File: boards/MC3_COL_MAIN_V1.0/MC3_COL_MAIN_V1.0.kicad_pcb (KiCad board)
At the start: 4 copper layers, 66 x 66 mm, 0 parts

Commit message: PCB: 101 footprints imported from the schematic via Konnect update_pcb_from_schematic (IPC), saved from KiCad; not yet placed
Co-Authored-By: Claude Fable 5 <noreply@anthropic.com>
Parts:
- added C1: 10uF, MC3_COL_MAIN:C_0805_2012Metric, F.Cu at (6.70, 25.0)
- added C10: 100nF, MC3_COL_MAIN:C_0402_1005Metric, F.Cu at (5.91, 154.6)
- added C11: 1uF, MC3_COL_MAIN:C_0402_1005Metric, F.Cu at (5.91, 160.6)
- added C12: 33pF, MC3_COL_MAIN:C_0402_1005Metric, F.Cu at (5.91, 166.6)
- added C13: 100nF, MC3_COL_MAIN:C_0402_1005Metric, F.Cu at (5.91, 172.6)
- added C14: 4.7uF, MC3_COL_MAIN:C_0603_1608Metric, F.Cu at (6.48, 178.9)
- added C15: 100nF, MC3_COL_MAIN:C_0402_1005Metric, F.Cu at (5.91, 185.1)
- added C16: 4.7uF, MC3_COL_MAIN:C_0805_2012Metric, F.Cu at (6.70, 191.6)
- added C17: 4.7uF, MC3_COL_MAIN:C_0603_1608Metric, F.Cu at (6.48, 350.0)
- added C18: 1uF, MC3_COL_MAIN:C_0603_1608Metric, F.Cu at (6.48, 434.1)
- added C19: 100nF, MC3_COL_MAIN:C_0402_1005Metric, F.Cu at (5.91, 440.3)
- added C2: 22uF 10V Ta, MC3_COL_MAIN:CP_EIA-3216-18_Kemet-A, F.Cu at (7.31, 32.0)
- added C20: 1uF, MC3_COL_MAIN:C_0603_1608Metric, F.Cu at (6.48, 483.7)
- added C21: 100nF, MC3_COL_MAIN:C_0402_1005Metric, F.Cu at (5.91, 489.9)
- added C22: 1uF, MC3_COL_MAIN:C_0603_1608Metric, F.Cu at (6.48, 533.3)
- added C23: 100nF, MC3_COL_MAIN:C_0402_1005Metric, F.Cu at (5.91, 539.6)
- added C24: 1uF, MC3_COL_MAIN:C_0603_1608Metric, F.Cu at (6.48, 582.9)
- added C25: 100nF, MC3_COL_MAIN:C_0402_1005Metric, F.Cu at (5.91, 589.2)
- added C26: 1uF, MC3_COL_MAIN:C_0603_1608Metric, F.Cu at (6.48, 632.6)
- added C27: 100nF, MC3_COL_MAIN:C_0402_1005Metric, F.Cu at (5.91, 638.8)
- added C28: 100nF, MC3_COL_MAIN:C_0402_1005Metric, F.Cu at (5.91, 682.0)
- added C29: 4.7uF, MC3_COL_MAIN:C_0603_1608Metric, F.Cu at (6.48, 688.2)
- added C3: 22uF 25V, MC3_COL_MAIN:C_0805_2012Metric, F.Cu at (6.70, 39.0)
- added C30: 4.7nF, MC3_COL_MAIN:C_0402_1005Metric, F.Cu at (5.91, 694.4)
- added C4: 22uF 25V, MC3_COL_MAIN:C_0805_2012Metric, F.Cu at (6.70, 46.0)
- added C5: 100nF, MC3_COL_MAIN:C_0402_1005Metric, F.Cu at (5.91, 124.6)
- added C6: 100nF, MC3_COL_MAIN:C_0402_1005Metric, F.Cu at (5.91, 130.6)
- added C7: 100nF, MC3_COL_MAIN:C_0402_1005Metric, F.Cu at (5.91, 136.6)
- added C8: 33pF, MC3_COL_MAIN:C_0402_1005Metric, F.Cu at (5.91, 142.6)
- added C9: 100nF, MC3_COL_MAIN:C_0402_1005Metric, F.Cu at (5.91, 148.6)
- added D1: SMAJ5.0A, MC3_COL_MAIN:D_SMA, F.Cu at (8.50, 54.4)
- added D2: LED_GREEN, MC3_COL_MAIN:LED_0603_1608Metric, F.Cu at (6.48, 198.3)
- added D3: LED_RED, MC3_COL_MAIN:LED_0603_1608Metric, F.Cu at (6.48, 204.8)
- added D4: PESD1CAN, MC3_COL_MAIN:SOT-23, F.Cu at (6.93, 701.6)
- added F1: 2A hold/3.5A trip, MC3_COL_MAIN:Fuse_1206_3216Metric, F.Cu at (7.28, 62.9)
- added FB1: 600R@100MHz, MC3_COL_MAIN:L_0603_1608Metric, F.Cu at (6.48, 211.2)
- added FB2: 600R@100MHz, MC3_COL_MAIN:L_0603_1608Metric, F.Cu at (6.48, 356.4)
- added FB3: 600R@100MHz, MC3_COL_MAIN:L_0603_1608Metric, F.Cu at (6.48, 709.0)
- added J1: SUPPLY_IN, MC3_COL_MAIN:SolderPads_2x_3.5x2.0mm_P4.2mm, F.Cu at (9.32, 71.7)
- added J10: MOTOR, MC3_COL_MAIN:SolderPads_2x_2.2x1.4mm_P2.6mm, F.Cu at (7.88, 597.1)
- added J11: MOTOR, MC3_COL_MAIN:SolderPads_2x_2.2x1.4mm_P2.6mm, F.Cu at (7.88, 646.8)
- added J12: CAN, MC3_COL_MAIN:SolderPads_3x_2.2x1.4mm_P2.6mm, F.Cu at (9.18, 717.2)
- added J2: SWD, MC3_COL_MAIN:PinHeader_1x06_P2.54mm_Vertical, F.Cu at (6.77, 225.1)
- added J3: ENC_leaf1, MC3_COL_MAIN:Panasonic_AYF530435_FFC-4P_P0.5mm, F.Cu at (7.20, 365.6)
- added J4: ENC_leaf2, MC3_COL_MAIN:Panasonic_AYF530435_FFC-4P_P0.5mm, F.Cu at (7.20, 377.4)
- added J5: ENC_leaf3, MC3_COL_MAIN:Panasonic_AYF530435_FFC-4P_P0.5mm, F.Cu at (7.20, 389.2)
- added J6: ENC_leaf4, MC3_COL_MAIN:Panasonic_AYF530435_FFC-4P_P0.5mm, F.Cu at (7.20, 401.0)
- added J7: MOTOR, MC3_COL_MAIN:SolderPads_2x_2.2x1.4mm_P2.6mm, F.Cu at (7.88, 448.3)
- added J8: MOTOR, MC3_COL_MAIN:SolderPads_2x_2.2x1.4mm_P2.6mm, F.Cu at (7.88, 497.9)
- added J9: MOTOR, MC3_COL_MAIN:SolderPads_2x_2.2x1.4mm_P2.6mm, F.Cu at (7.88, 547.5)
- added Q1: AO4407C, MC3_COL_MAIN:SOIC-8_3.9x4.9mm_P1.27mm, F.Cu at (8.70, 82.2)
- added R1: 2.2k, MC3_COL_MAIN:R_0402_1005Metric, F.Cu at (5.93, 0.50)
- added R10: 1k, MC3_COL_MAIN:R_0402_1005Metric, F.Cu at (5.93, 262.7)
- added R11: 1k, MC3_COL_MAIN:R_0402_1005Metric, F.Cu at (5.93, 268.7)
- added R12: 10k, MC3_COL_MAIN:R_0402_1005Metric, F.Cu at (5.93, 409.9)
- added R13: 10k, MC3_COL_MAIN:R_0402_1005Metric, F.Cu at (5.93, 415.9)
- added R14: 10k, MC3_COL_MAIN:R_0402_1005Metric, F.Cu at (5.93, 421.9)
- added R15: 10k, MC3_COL_MAIN:R_0402_1005Metric, F.Cu at (5.93, 427.9)
- added R16: 6.8k, MC3_COL_MAIN:R_0402_1005Metric, F.Cu at (5.93, 456.2)
- added R17: 10k, MC3_COL_MAIN:R_0402_1005Metric, F.Cu at (5.93, 462.2)
- added R18: 10k, MC3_COL_MAIN:R_0402_1005Metric, F.Cu at (5.93, 468.2)
- added R19: 6.8k, MC3_COL_MAIN:R_0402_1005Metric, F.Cu at (5.93, 505.8)
- added R2: 2.2k, MC3_COL_MAIN:R_0402_1005Metric, F.Cu at (5.93, 6.50)
- added R20: 10k, MC3_COL_MAIN:R_0402_1005Metric, F.Cu at (5.93, 511.8)
- added R21: 10k, MC3_COL_MAIN:R_0402_1005Metric, F.Cu at (5.93, 517.8)
- added R22: 6.8k, MC3_COL_MAIN:R_0402_1005Metric, F.Cu at (5.93, 555.5)
- added R23: 10k, MC3_COL_MAIN:R_0402_1005Metric, F.Cu at (5.93, 561.5)
- added R24: 10k, MC3_COL_MAIN:R_0402_1005Metric, F.Cu at (5.93, 567.5)
- added R25: 6.8k, MC3_COL_MAIN:R_0402_1005Metric, F.Cu at (5.93, 605.1)
- added R26: 10k, MC3_COL_MAIN:R_0402_1005Metric, F.Cu at (5.93, 611.1)
- added R27: 10k, MC3_COL_MAIN:R_0402_1005Metric, F.Cu at (5.93, 617.1)
- added R28: 6.8k, MC3_COL_MAIN:R_0402_1005Metric, F.Cu at (5.93, 654.7)
- added R29: 10k, MC3_COL_MAIN:R_0402_1005Metric, F.Cu at (5.93, 660.7)
- added R3: 2.2k, MC3_COL_MAIN:R_0402_1005Metric, F.Cu at (5.93, 12.5)
- added R30: 10k, MC3_COL_MAIN:R_0402_1005Metric, F.Cu at (5.93, 666.7)
- added R31: 62R, MC3_COL_MAIN:R_0402_1005Metric, F.Cu at (5.93, 725.2)
- added R32: 62R, MC3_COL_MAIN:R_0402_1005Metric, F.Cu at (5.93, 731.2)
- added R4: 2.2k, MC3_COL_MAIN:R_0402_1005Metric, F.Cu at (5.93, 18.5)
- added R5: 100k, MC3_COL_MAIN:R_0402_1005Metric, F.Cu at (5.93, 90.5)
- added R6: 4.7k, MC3_COL_MAIN:R_0402_1005Metric, F.Cu at (5.93, 238.7)
- added R7: 4.7k, MC3_COL_MAIN:R_0402_1005Metric, F.Cu at (5.93, 244.7)
- added R72: 0R, MC3_COL_MAIN:R_0402_1005Metric, F.Cu at (5.93, 737.2)
- added R8: 10k, MC3_COL_MAIN:R_0402_1005Metric, F.Cu at (5.93, 250.7)
- added R9: 10k, MC3_COL_MAIN:R_0402_1005Metric, F.Cu at (5.93, 256.7)
- added SW1: SKRKAEE020, MC3_COL_MAIN:SW_Push_SPST_NO_Alps_SKRK, F.Cu at (7.75, 275.9)
- added TP1: VM, MC3_COL_MAIN:TestPoint_Pad_1.0x1.0mm, F.Cu at (6.00, 97.5)
- added TP2: VIN_PROT, MC3_COL_MAIN:TestPoint_Pad_1.0x1.0mm, F.Cu at (6.00, 105.4)
- added TP3: +3V3, MC3_COL_MAIN:TestPoint_Pad_1.0x1.0mm, F.Cu at (6.00, 284.1)
- added TP4: SCL, MC3_COL_MAIN:TestPoint_Pad_1.0x1.0mm, F.Cu at (6.00, 292.0)
- added TP5: SDA, MC3_COL_MAIN:TestPoint_Pad_1.0x1.0mm, F.Cu at (6.00, 300.0)
- added TP6: IPROPI1, MC3_COL_MAIN:TestPoint_Pad_1.0x1.0mm, F.Cu at (6.00, 307.9)
- added TP7: GND, MC3_COL_MAIN:TestPoint_Pad_1.0x1.0mm, F.Cu at (6.00, 315.9)
- added U1: AMS1117-3.3, MC3_COL_MAIN:SOT-223-3_TabPin2, F.Cu at (9.40, 115.5)
- added U2: STM32F412RET6, MC3_COL_MAIN:LQFP-64_10x10mm_P0.5mm, F.Cu at (11.7, 329.0)
- added U3: DRV8214RTER, MC3_COL_MAIN:WQFN-16-1EP_3x3mm_P0.5mm_EP1.68x1.68mm_ThermalVias, F.Cu at (7.30, 475.8)
- added U4: DRV8214RTER, MC3_COL_MAIN:WQFN-16-1EP_3x3mm_P0.5mm_EP1.68x1.68mm_ThermalVias, F.Cu at (7.30, 525.5)
- added U5: DRV8214RTER, MC3_COL_MAIN:WQFN-16-1EP_3x3mm_P0.5mm_EP1.68x1.68mm_ThermalVias, F.Cu at (7.30, 575.1)
- added U6: DRV8214RTER, MC3_COL_MAIN:WQFN-16-1EP_3x3mm_P0.5mm_EP1.68x1.68mm_ThermalVias, F.Cu at (7.30, 624.7)
- added U7: DRV8214RTER, MC3_COL_MAIN:WQFN-16-1EP_3x3mm_P0.5mm_EP1.68x1.68mm_ThermalVias, F.Cu at (7.30, 674.3)
- added U8: TJA1051T/3, MC3_COL_MAIN:SOIC-8_3.9x4.9mm_P1.27mm, F.Cu at (8.70, 745.4)
- added Y1: 8MHz, MC3_COL_MAIN:Crystal_SMD_3225-4Pin_3.2x2.5mm, F.Cu at (7.10, 342.5)

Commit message: PCB placement pass 1: all 101 footprints placed per the plan (MCU west, drivers beside their clusters, power/CAN east, yaw SE); courtyard-clean except thermal-via hole rule
Co-Authored-By: Claude Fable 5 <noreply@anthropic.com>
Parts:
- moved U8 639.7 mm to (123.0, 116.0)
- moved R72 639.3 mm to (125.5, 109.2)
- moved R32 630.4 mm to (125.5, 112.2)
- moved R31 626.0 mm to (125.5, 110.7)
- moved J12 623.7 mm to (127.6, 104.9), turned to 90 degrees
- moved FB3 608.5 mm to (116.2, 110.5)
- moved D4 606.4 mm to (124.7, 106.8), turned to 90 degrees
- moved C30 595.6 mm to (123.5, 110.5)
- moved C29 589.0 mm to (121.2, 110.5)
- moved C28 582.5 mm to (118.7, 110.5)
- moved U7 565.9 mm to (108.1, 117.5), turned to 45 degrees
- moved R30 556.4 mm to (112.0, 120.5)
- moved R29 549.3 mm to (113.2, 122.0)
- moved R28 548.6 mm to (112.0, 116.5), turned to 90 degrees
- moved J11 538.4 mm to (120.2, 120.2)
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
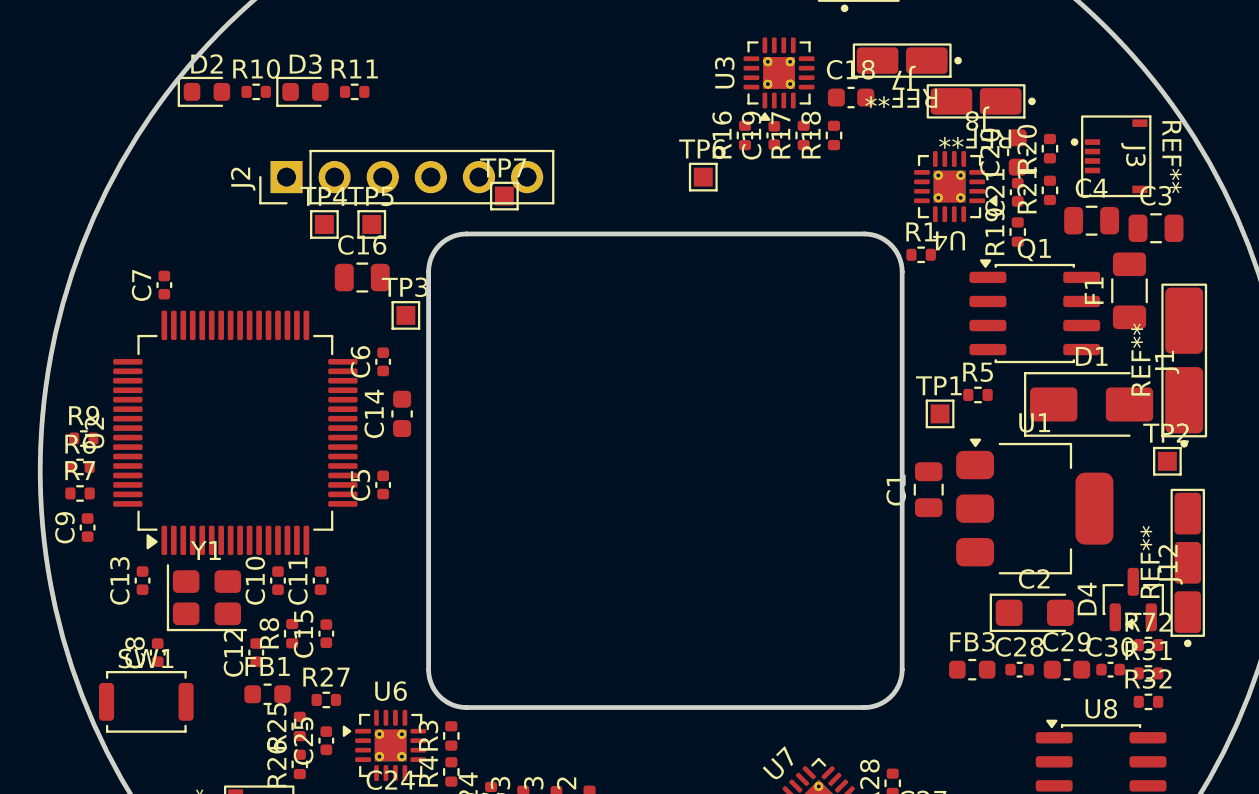
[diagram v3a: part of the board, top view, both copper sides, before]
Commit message: PCB placement pass 1 complete: SWD header on the west rim, remaining courtyard overlaps cleared; MIGRATION records placement + outstanding GUI items
Co-Authored-By: Claude Fable 5 <noreply@anthropic.com>
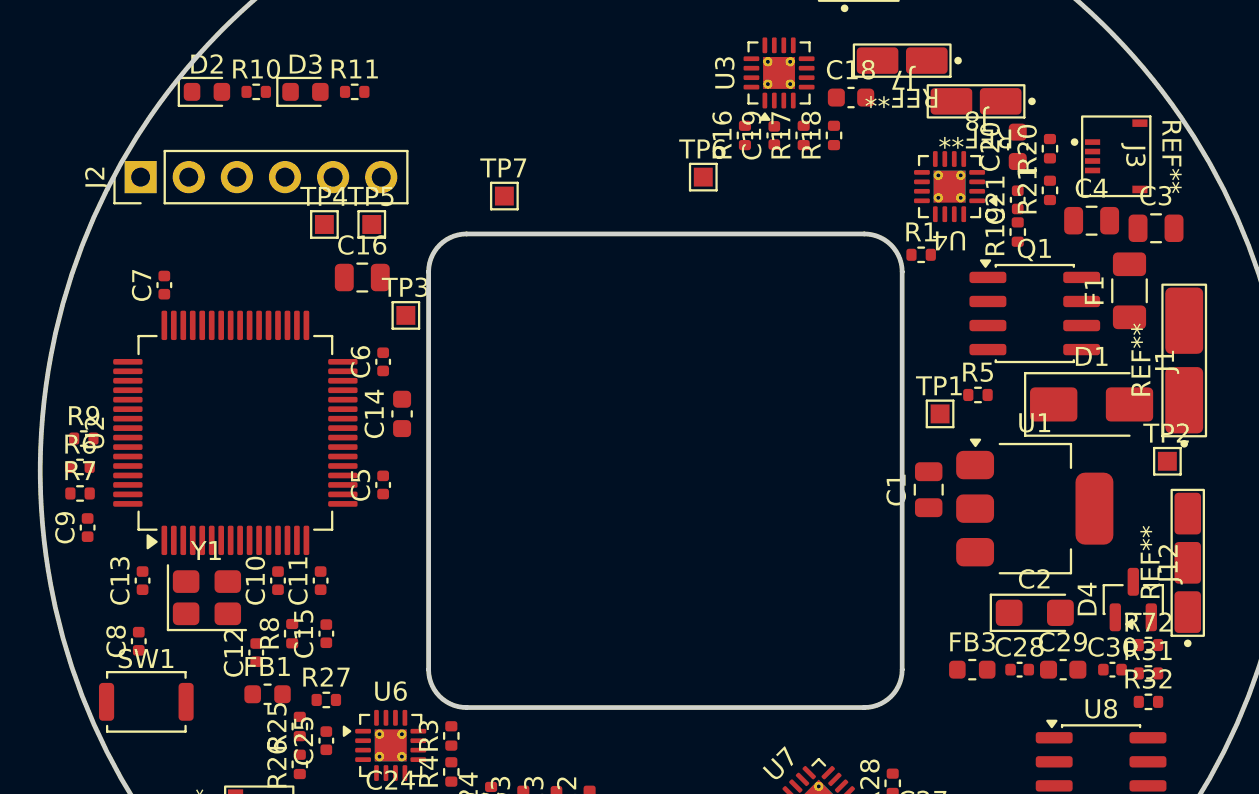
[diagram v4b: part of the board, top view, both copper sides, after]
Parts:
- moved J2 7.70 mm to (72.3, 84.5)
- moved C8 1.17 mm to (72.2, 109.0)
- moved C21 0.40 mm to (118.6, 85.7)
- moved C20 0.30 mm to (118.6, 82.9)
- moved C29 0.20 mm to (121.0, 110.5)
- moved C30 0.10 mm to (123.6, 110.5)
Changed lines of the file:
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@@
 	(footprint "MC3_COL_MAIN:C_0603_1608Metric"
 		(layer "F.Cu")
-		(at 118.6 83.2 90)
+		(at 118.6 82.9 90)
 		(property "Reference" "C20"
 			(at 0 -1.43 90)
@@
 	(footprint "MC3_COL_MAIN:C_0402_1005Metric"
 		(layer "F.Cu")
-		(at 118.6 85.3 90)
+		(at 118.6 85.7 90)
 		(property "Reference" "C21"
 			(at 0 -1.16 90)
@@
 	(footprint "MC3_COL_MAIN:PinHeader_1x06_P2.54mm_Vertical"
 		(layer "F.Cu")
-		(at 80 84.5 90)
+		(at 72.3 84.5 90)
 		(property "Reference" "J2"
 			(at 0 -2.38 90)
@@
 	(footprint "MC3_COL_MAIN:C_0402_1005Metric"
 		(layer "F.Cu")
-		(at 73.2 109.6 90)
+		(at 72.2 109 90)
 		(property "Reference" "C8"
 			(at 0 -1.16 90)
@@
 	(footprint "MC3_COL_MAIN:C_0402_1005Metric"
 		(layer "F.Cu")
-		(at 123.5 110.5)
+		(at 123.6 110.5)
 		(property "Reference" "C30"
 			(at 0 -1.16 0)
@@
 	(footprint "MC3_COL_MAIN:C_0603_1608Metric"
 		(layer "F.Cu")
-		(at 121.2 110.5)
+		(at 121 110.5)
 		(property "Reference" "C29"
 			(at 0 -1.43 0)

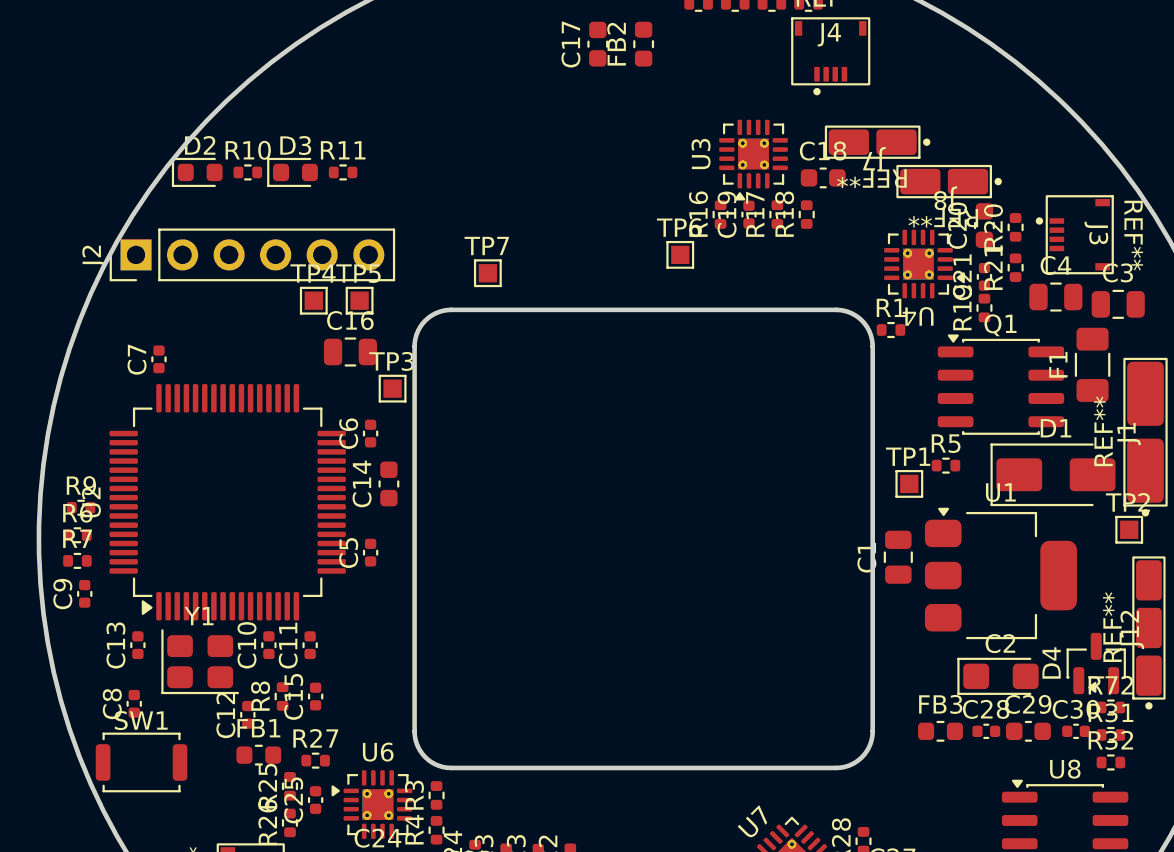
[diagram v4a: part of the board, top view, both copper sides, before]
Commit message: PCB placement: last courtyard/edge items cleared (U4/J7/J8 spread, SWD header inboard, TPs dropped)
Co-Authored-By: Claude Fable 5 <noreply@anthropic.com>
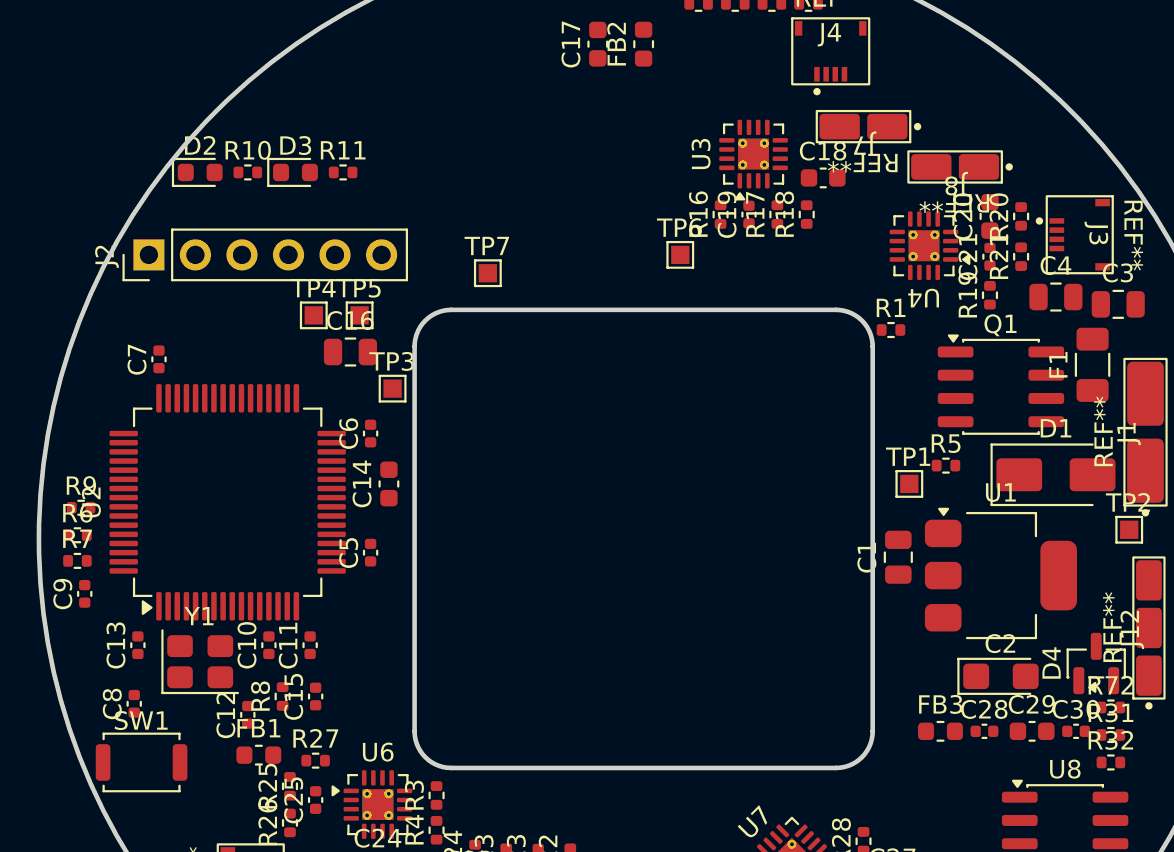
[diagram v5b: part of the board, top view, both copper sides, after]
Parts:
- moved C21 1.14 mm to (118.9, 84.6)
- moved U4 1.04 mm to (115.3, 84.0)
- moved J8 1.00 mm to (117.0, 79.7)
- moved J7 0.99 mm to (112.0, 77.5)
- moved TP4 0.80 mm to (82.0, 87.8)
- moved TP5 0.80 mm to (84.5, 87.8)
- moved R19 0.76 mm to (118.9, 86.7)
- moved J2 0.70 mm to (73.0, 84.5)
- moved R21 0.67 mm to (120.6, 84.6)
- moved R20 0.67 mm to (120.6, 82.4)
- moved C20 0.58 mm to (118.9, 82.4)
- moved C29 0.20 mm to (121.2, 110.5)
- moved C28 0.10 mm to (118.6, 110.5)
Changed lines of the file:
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@@
 	(footprint "MC3_COL_MAIN:C_0603_1608Metric"
 		(layer "F.Cu")
-		(at 118.6 82.9 90)
+		(at 118.9 82.4 90)
 		(property "Reference" "C20"
 			(at 0 -1.43 90)
@@
 	(footprint "MC3_COL_MAIN:TestPoint_Pad_1.0x1.0mm"
 		(layer "F.Cu")
-		(at 84.5 87)
+		(at 84.5 87.8)
 		(property "Reference" "TP5"
 			(at 0 -1.448 0)
@@
 	(footprint "MC3_COL_MAIN:SolderPads_2x_2.2x1.4mm_P2.6mm"
 		(layer "F.Cu")
-		(at 116.4 80.5 180)
+		(at 117 79.7 180)
 		(property "Reference" "J8"
 			(at 0 -1 180)
@@
 	(footprint "MC3_COL_MAIN:C_0402_1005Metric"
 		(layer "F.Cu")
-		(at 118.7 110.5)
+		(at 118.6 110.5)
 		(property "Reference" "C28"
 			(at 0 -1.159999 0)
@@
 	(footprint "MC3_COL_MAIN:R_0402_1005Metric"
 		(layer "F.Cu")
-		(at 120.3 83 90)
+		(at 120.6 82.4 90)
 		(property "Reference" "R20"
 			(at 0 -1.17 90)
@@
 	(footprint "MC3_COL_MAIN:SolderPads_2x_2.2x1.4mm_P2.6mm"
 		(layer "F.Cu")
-		(at 112.5 78.35 180)
+		(at 112 77.5 180)
 		(property "Reference" "J7"
 			(at 0 -1 180)
@@
 	(footprint "MC3_COL_MAIN:C_0402_1005Metric"
 		(layer "F.Cu")
-		(at 118.6 85.7 90)
+		(at 118.9 84.6 90)
 		(property "Reference" "C21"
 			(at 0 -1.16 90)
@@
 	(footprint "MC3_COL_MAIN:R_0402_1005Metric"
 		(layer "F.Cu")
-		(at 120.3 85.2 90)
+		(at 120.6 84.6 90)
 		(property "Reference" "R21"
 			(at 0 -1.17 90)
@@
 	(footprint "MC3_COL_MAIN:PinHeader_1x06_P2.54mm_Vertical"
 		(layer "F.Cu")
-		(at 72.3 84.5 90)
+		(at 73 84.5 90)
 		(property "Reference" "J2"
 			(at 0 -2.38 90)
@@
 	(footprint "MC3_COL_MAIN:WQFN-16-1EP_3x3mm_P0.5mm_EP1.68x1.68mm_ThermalVias"
 		(layer "F.Cu")
-		(at 115 85 180)
+		(at 115.3 84 180)
 		(property "Reference" "U4"
 			(at 0 -2.83 180)
@@
 	(footprint "MC3_COL_MAIN:TestPoint_Pad_1.0x1.0mm"
 		(layer "F.Cu")
-		(at 82 87)
+		(at 82 87.8)
 		(property "Reference" "TP4"
 			(at 0 -1.448 0)
@@
 	(footprint "MC3_COL_MAIN:R_0402_1005Metric"
 		(layer "F.Cu")
-		(at 118.6 87.4 90)
+		(at 118.9 86.7 90)
 		(property "Reference" "R19"
 			(at 0 -1.17 90)
@@
 	(footprint "MC3_COL_MAIN:C_0603_1608Metric"
 		(layer "F.Cu")
-		(at 121 110.5)
+		(at 121.2 110.5)
 		(property "Reference" "C29"
 			(at 0 -1.43 0)

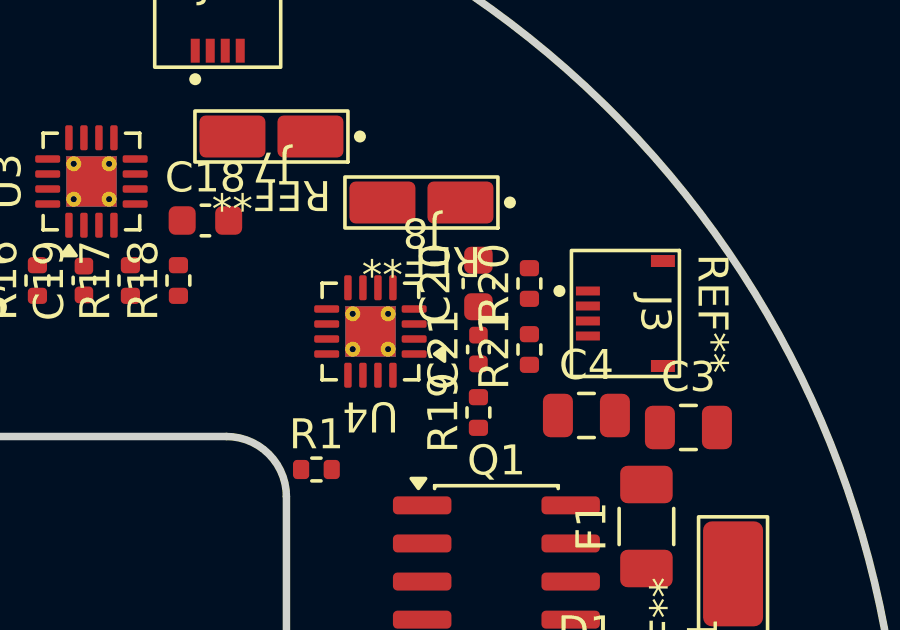
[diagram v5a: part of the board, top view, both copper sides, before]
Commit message: PCB placement: C20/C21 pitch; placement pass 1 courtyard-clean (only the 0.2 mm thermal-via hole rule outstanding)
Co-Authored-By: Claude Fable 5 <noreply@anthropic.com>
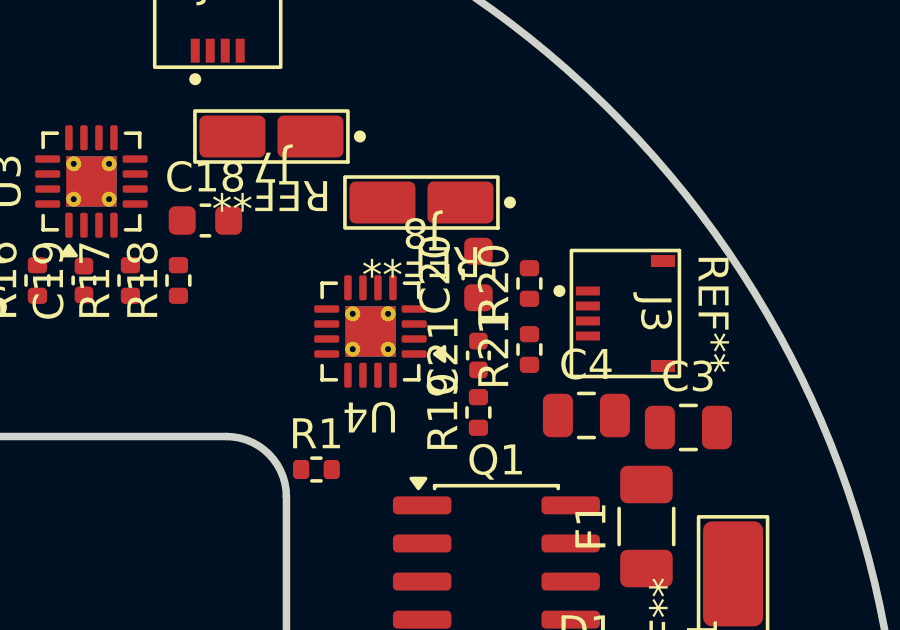
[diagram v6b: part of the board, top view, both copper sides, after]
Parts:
- moved C20 0.30 mm to (118.9, 82.1)
- moved C21 0.20 mm to (118.9, 84.8)
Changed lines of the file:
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@@
 	(footprint "MC3_COL_MAIN:C_0603_1608Metric"
 		(layer "F.Cu")
-		(at 118.9 82.4 90)
+		(at 118.9 82.1 90)
 		(property "Reference" "C20"
 			(at 0 -1.43 90)
@@
 	(footprint "MC3_COL_MAIN:C_0402_1005Metric"
 		(layer "F.Cu")
-		(at 118.9 84.6 90)
+		(at 118.9 84.8 90)
 		(property "Reference" "C21"
 			(at 0 -1.16 90)
